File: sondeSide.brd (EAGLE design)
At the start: 104.6 x 31.8 mm, 42 parts

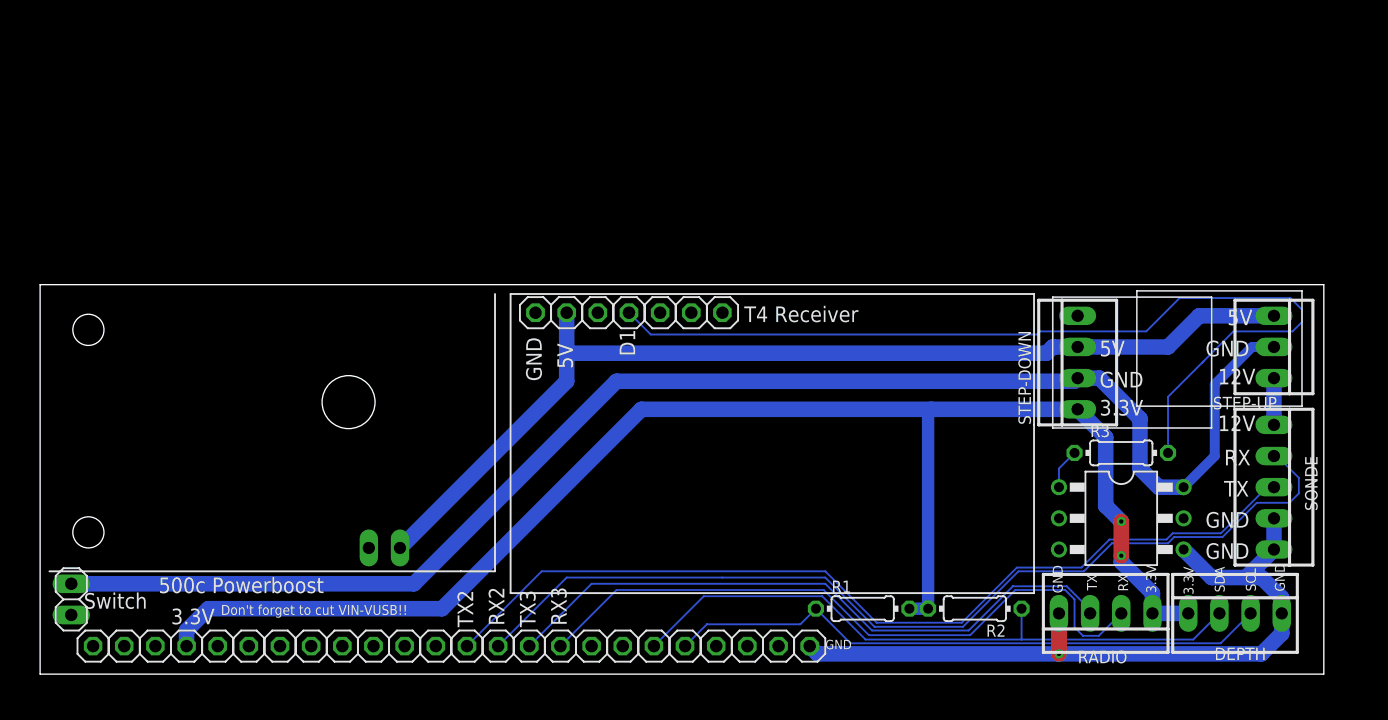
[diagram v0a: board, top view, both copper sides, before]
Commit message: Electrically ready to go
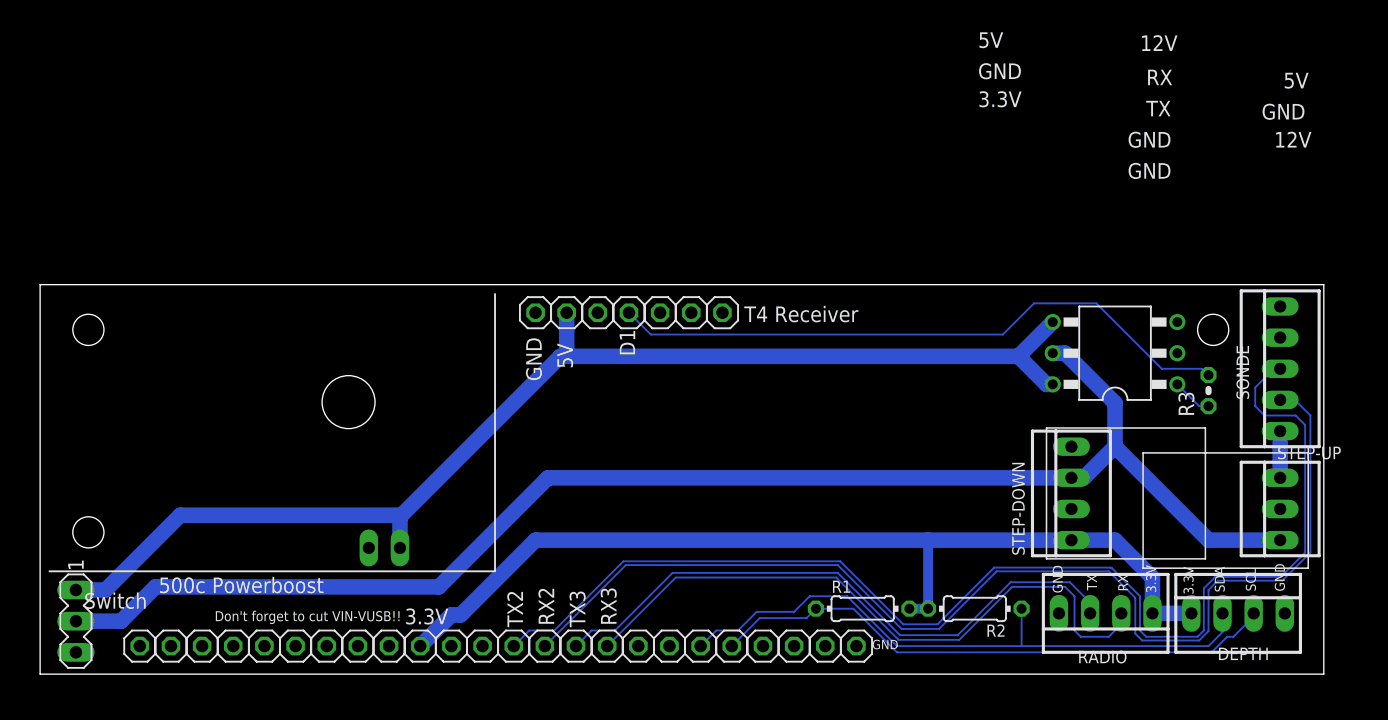
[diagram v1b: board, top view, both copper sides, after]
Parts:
- JP25: device pinhead:1X02 -> con-lstb:MA03-1
- R3: device rcl:0204/7 -> rcl:0204V
- moved JP13 21.6 mm to (36.1, 2.29)
- moved JP15 19.0 mm to (31.0, 2.29)
- moved JP17 16.5 mm to (25.9, 2.29)
- moved JP19 14.0 mm to (20.8, 2.29)
- moved OK1 13.5 mm to (87.6, 26.2), turned to 90 degrees
- moved STEP-UP 13.2 mm to (101.1, 13.5), turned to 90 degrees
- moved JP21 11.4 mm to (15.7, 2.29)
- moved STEP-DOWN 10.7 mm to (84.1, 14.7)
- moved SONDE 9.67 mm to (101.1, 24.9), turned to 90 degrees
- moved JP23 8.89 mm to (10.7, 2.29)
- moved JP24 8.89 mm to (8.13, 2.29)
- moved JP22 8.89 mm to (13.2, 2.29)
- moved R3 8.74 mm to (95.2, 23.1), turned to 90 degrees
- moved JP20 6.35 mm to (18.3, 2.29)
- moved JP1 3.81 mm to (66.5, 2.29)
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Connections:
- removed net GND_PLANE: JP25.2, JP26.1, OK1.2, OK1.5, PWRBOOST.1
- new net 5V_TO_SMPS: JP25.2, OK1.5, STEP-DOWN.3, STEP-UP.1
- net 5V: now also JP25.1, OK1.4, OK1.6; no longer STEP-DOWN.3, STEP-UP.1
- net GND: now also JP26.1, OK1.2, PWRBOOST.1; no longer JP25.1, OK1.4, OK1.6
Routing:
- net GND: track 181.7 -> 0.00 mm, vias 1 -> 0
- net 5V_TO_SMPS: track 0.00 -> 117.5 mm
- net 3.3V: track 124.9 -> 77.7 mm, vias 2 -> 0
- net D1: track 76.4 -> 51.5 mm
- net TX2: track 74.7 -> 99.5 mm
- net 5V: track 83.5 -> 98.7 mm
- net RX2: track 77.8 -> 92.4 mm
- net SCL: track 49.5 -> 46.7 mm
- net TX3: track 52.0 -> 49.8 mm
- net SDA: track 52.6 -> 51.0 mm
- net RX3: track 54.3 -> 52.7 mm

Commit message: Done with labels! Just would like to increase clearance on the ground pane
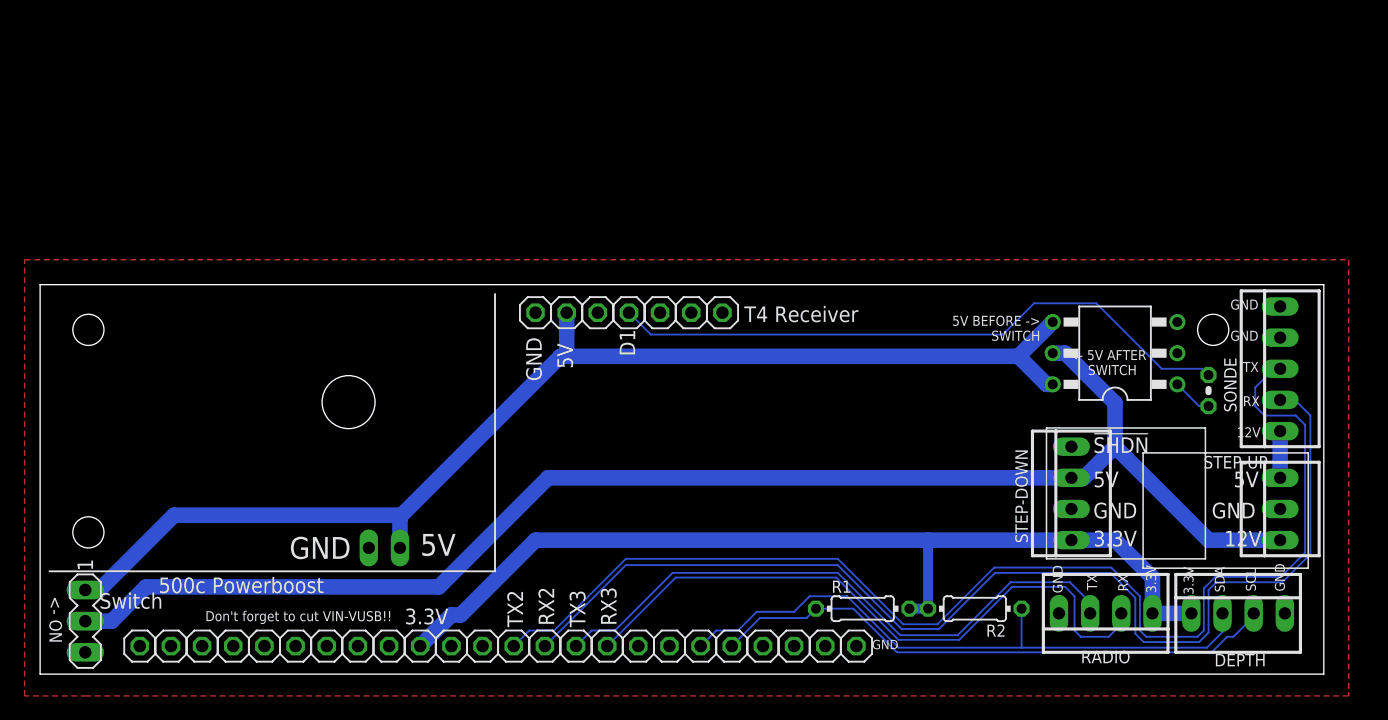
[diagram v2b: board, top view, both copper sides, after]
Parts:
- moved JP25 0.76 mm to (3.68, 4.32)
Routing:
- net 5V_TO_SMPS: track 117.5 -> 116.8 mm
- net 5V: track 98.7 -> 98.0 mm
- added copper zone on layer 1, net GND
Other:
- board text added: "!SHDN"
- board text added: "5V AFTER -> SWITCH"
- board text added: "5V BEFORE -> SWITCH"
- board text added: "<- 5V AFTER SWITCH"
- board text added: "<- 5V BEFORE SWITCH"
- board text added: "<- ON"
- board text added: "D0"
- board text added: "D2"
- board text added: "D3"
- board text added: "ON ->"
- board text added: "STEP-DOWN"
- board text added: "STEP-UP"
- board text added: "V1 NOV 2018"
- board text added: "VT"
- board text removed: "V1 OCT 2018"
